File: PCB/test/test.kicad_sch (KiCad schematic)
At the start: 63 parts, among them U1 STM32WBxx_QFN48, U2 USBLC6-2SC6, U3 LD3985M33R, U4 SFH_7072, X1 NX2016_32MHz, X2 NX2012_32K768Hz

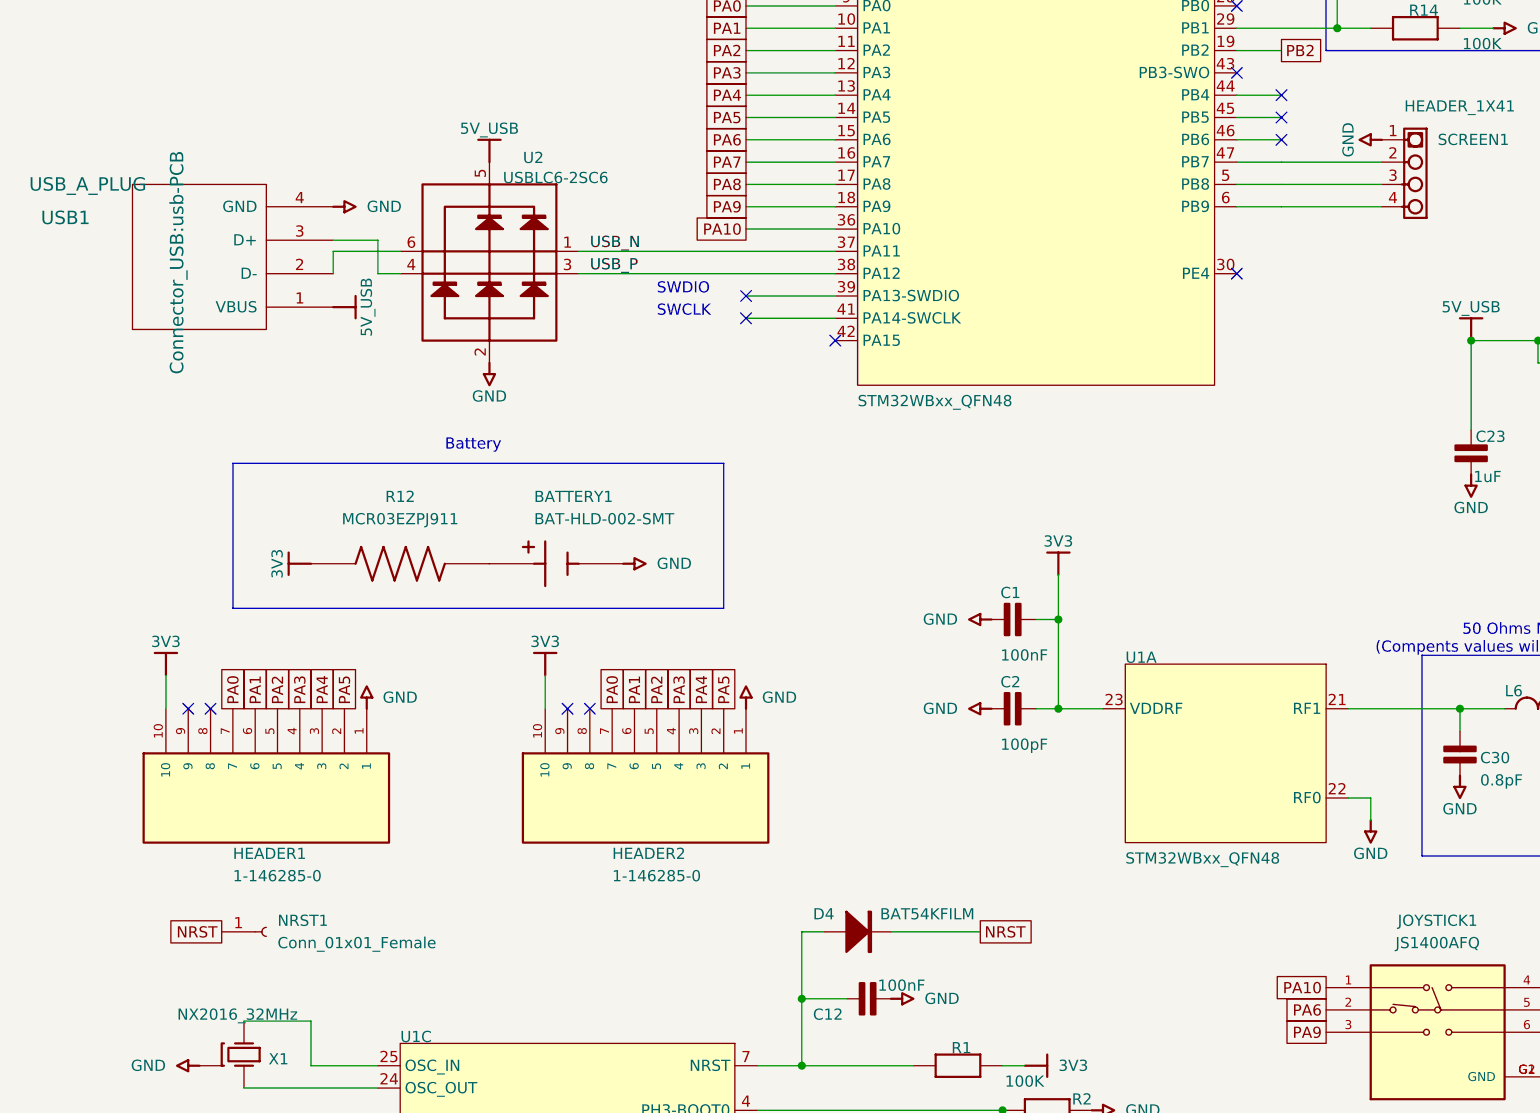
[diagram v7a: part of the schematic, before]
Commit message: ajout i2c
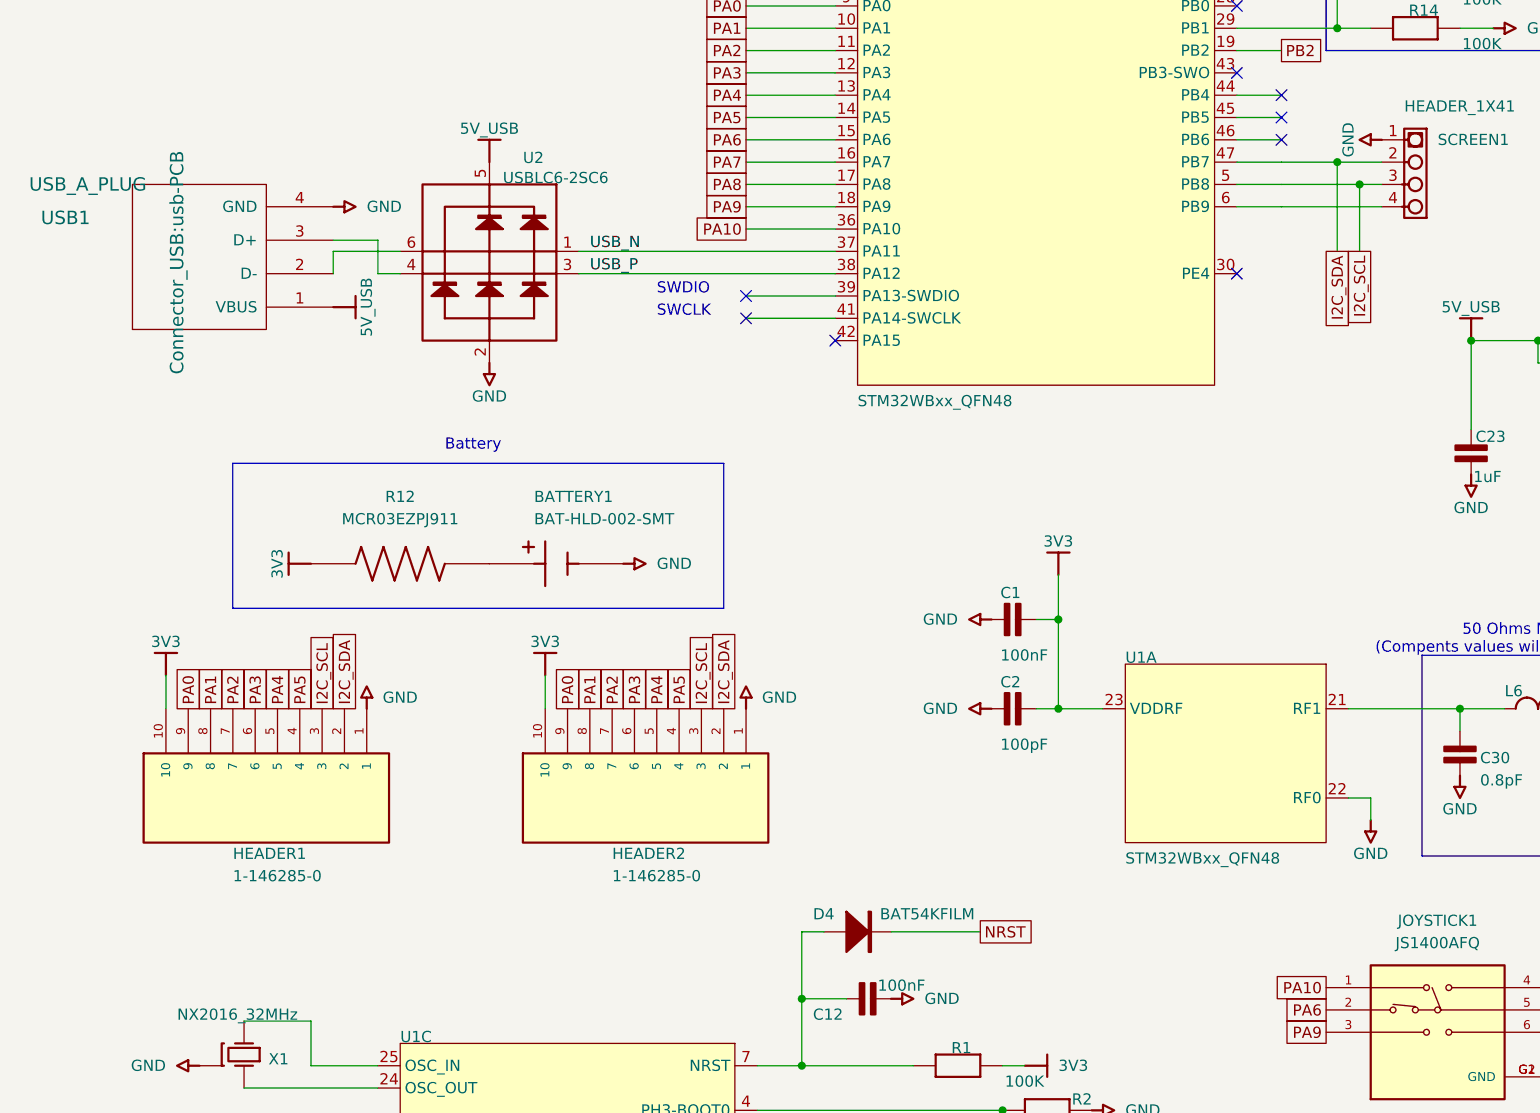
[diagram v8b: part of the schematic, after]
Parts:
- removed NRST1: Conn_01x01_Female, Connector_PinHeader_2.54mm:PinHeader_1x01_P2.54mm_Vertical, symbol Connector:Conn_01x01_Female
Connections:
- net PA0: now also HEADER1.9, HEADER2.9; no longer HEADER1.7, HEADER2.7
- net PA1: now also HEADER1.8, HEADER2.8; no longer HEADER1.6, HEADER2.6
- net PA2: now also HEADER1.7, HEADER2.7; no longer HEADER1.5, HEADER2.5
- net PA3: now also HEADER1.6, HEADER2.6; no longer HEADER1.4, HEADER2.4
- net PA4: now also HEADER1.5, HEADER2.5; no longer HEADER1.3, HEADER2.3
- net PA5: now also HEADER1.4, HEADER2.4; no longer HEADER1.2, HEADER2.2
- net I2C_SDA: now reaches SCREEN1.2, U1.47 (PB7)
- net I2C_SDA: now also HEADER1.2, HEADER2.2
- net I2C_SCL: now reaches SCREEN1.3, U1.5 (PB8)
- net I2C_SCL: now also HEADER1.3, HEADER2.3
- no-connect marks 15 -> 11
